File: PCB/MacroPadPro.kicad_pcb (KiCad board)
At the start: 2 copper layers, 160.7 x 77.6 mm, 119 parts, among them J1 Button, J2 Button, SW1 CPG151101S11, SW10 CPG151101S11, SW11 CPG151101S11, SW12 CPG151101S11, SW13 CPG151101S11, SW14 CPG151101S11, SW15 CPG151101S11, SW16 CPG151101S11, SW17 CPG151101S11, SW18 CPG151101S11, SW19 CPG151101S11, SW2 CPG151101S11, SW20 CPG151101S11, SW21 CPG151101S11, SW22 CPG151101S11, SW23 CPG151101S11, SW24 CPG151101S11, SW25 CPG151101S11, SW26 CPG151101S11, SW27 CPG151101S11, SW3 CPG151101S11, SW4 CPG151101S11, SW5 CPG151101S11, SW6 CPG151101S11, SW7 CPG151101S11, SW8 CPG151101S11, SW9 CPG151101S11, U1 ZL6201A33S3, U3 RP2040, Y1 TAXM12M4RKDCDT2T

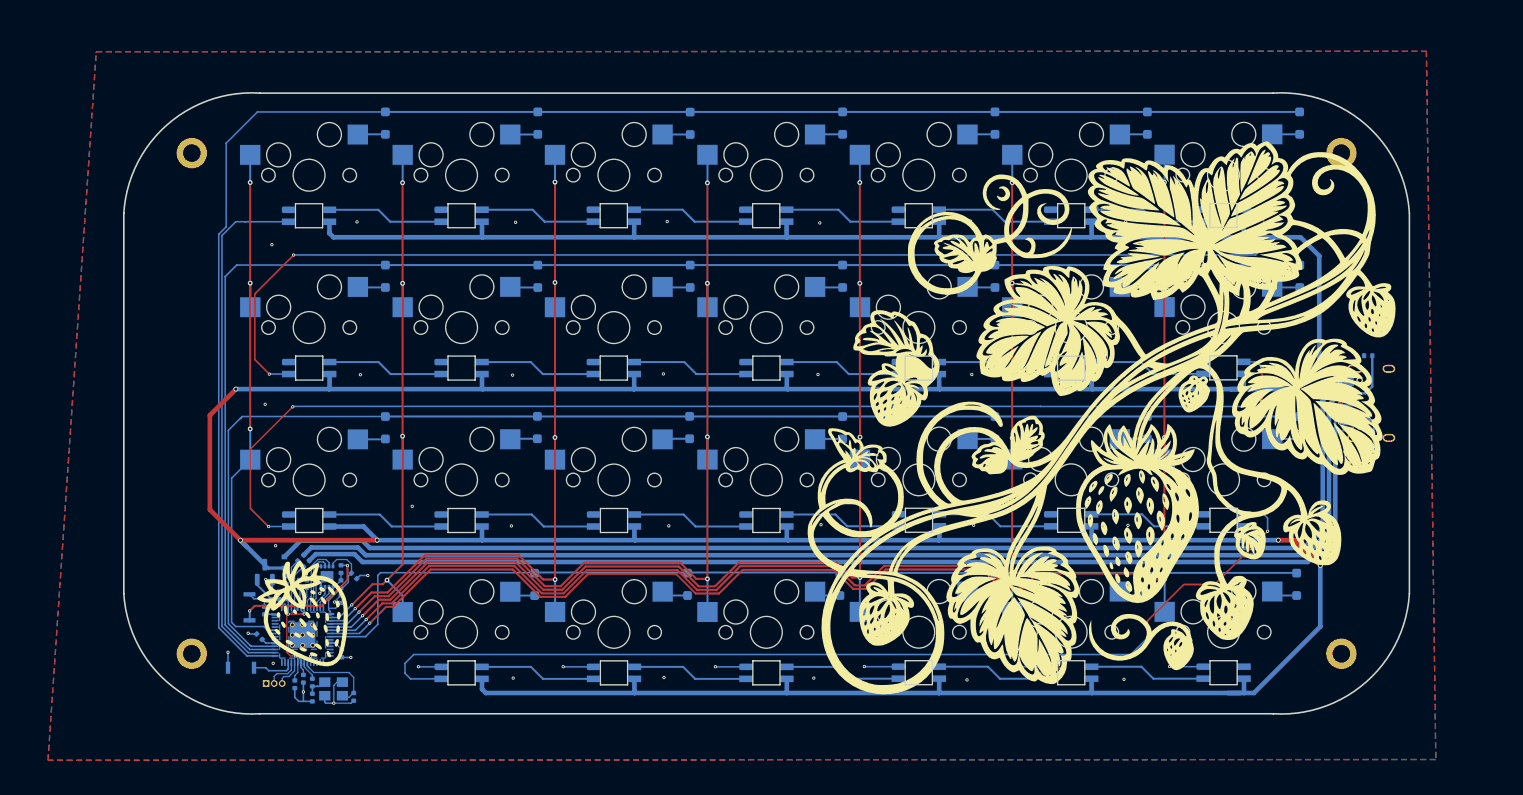
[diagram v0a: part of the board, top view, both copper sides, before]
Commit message: Updated PCB and added BOM
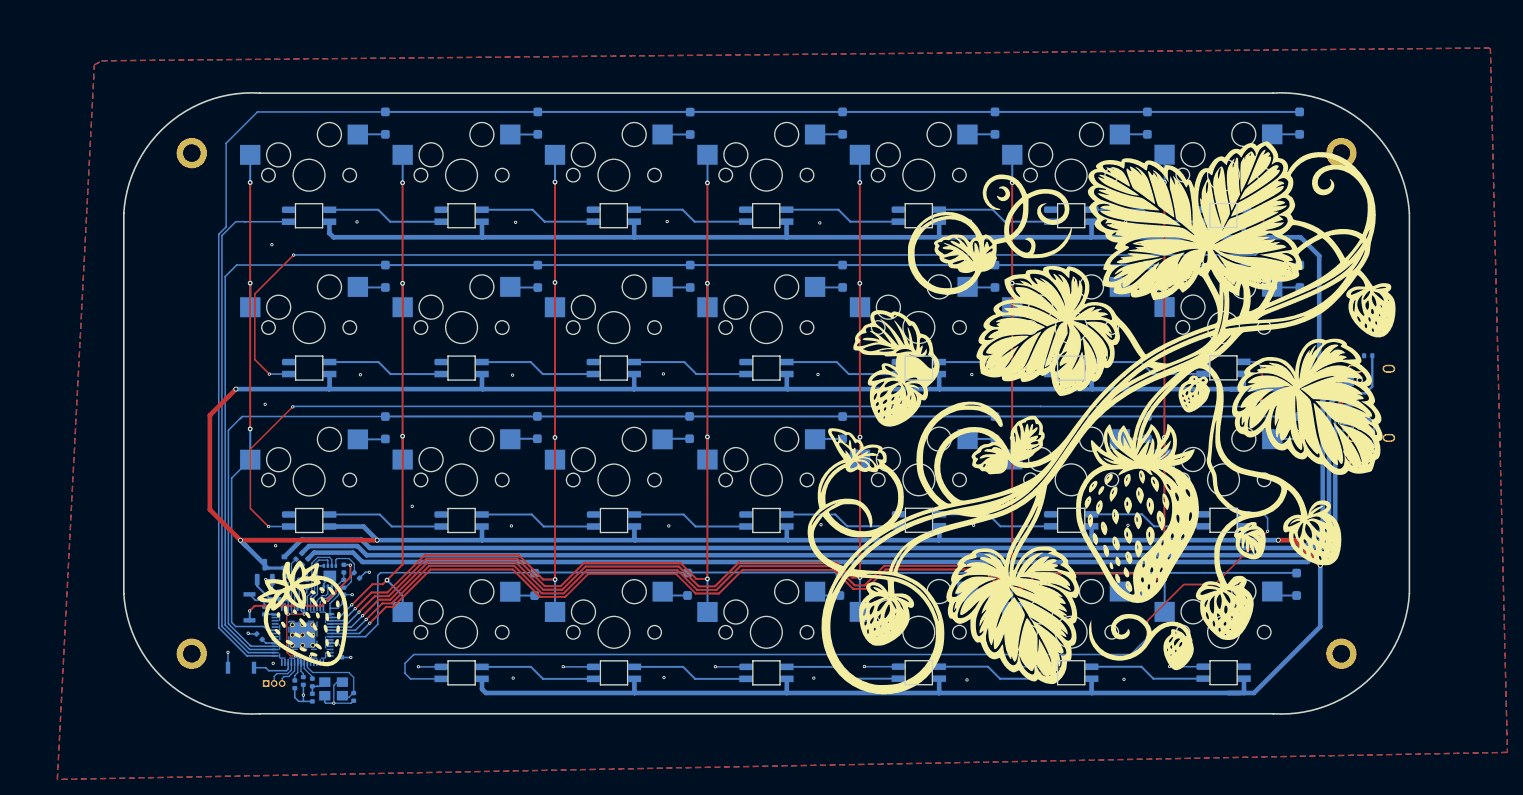
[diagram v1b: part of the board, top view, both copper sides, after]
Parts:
- C1, C10, C3, C4: value 1uf 0201 -> GRT033R60J105ME13D
- C11, C13, C14, C15, C18, C5, C6, C7, C8: value 100nf 0201 -> CSA0201X5R104K6R3ET
- C19: value 22pf 0402 -> GJM1555C1H220JB01D
- C2: value 22pF 0402 -> GJM1555C1H220JB01D
- D1: value SOD-523 General -> RB520SM-40T2R
- J1, J2: value Button -> KXT331LHS
- R1, R7: value 1K 0201 -> 0201WMF1001TEE
- R2: value 10K 0201 -> 0201WMF1002TEE
- R3, R4: value 27r 0201 -> 0201WMJ0270TEE
- R5, R6: value 5.1K 0201 -> RTT01512JTH
- hole (x4): renamed from ?; value (none) -> hole
- pin: renamed from REF**; value PinHeader_1x03_P1.00mm_Vertical -> DNP
- moved C5 0.36 mm to (107.0, 129.2)
- moved C15 0.36 mm to (105.4, 132.1)
- moved FLASH1 0.36 mm to (103.6, 129.3)
- moved R1 0.36 mm to (105.4, 128.4)
- moved R2 0.36 mm to (105.4, 130.3)
- moved R4 0.32 mm to (99.8, 126.8)
- moved R3 0.28 mm to (100.5, 127.5)
- moved C18 0.28 mm to (100.3, 142.4)
- moved C6 0.06 mm to (100.8, 130.3)
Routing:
- net +3V3: track 29.4 -> 30.8 mm
- net /QSPI_SD3: track 8.56 -> 9.48 mm
- net /QSPI_SCLK: track 7.34 -> 8.18 mm

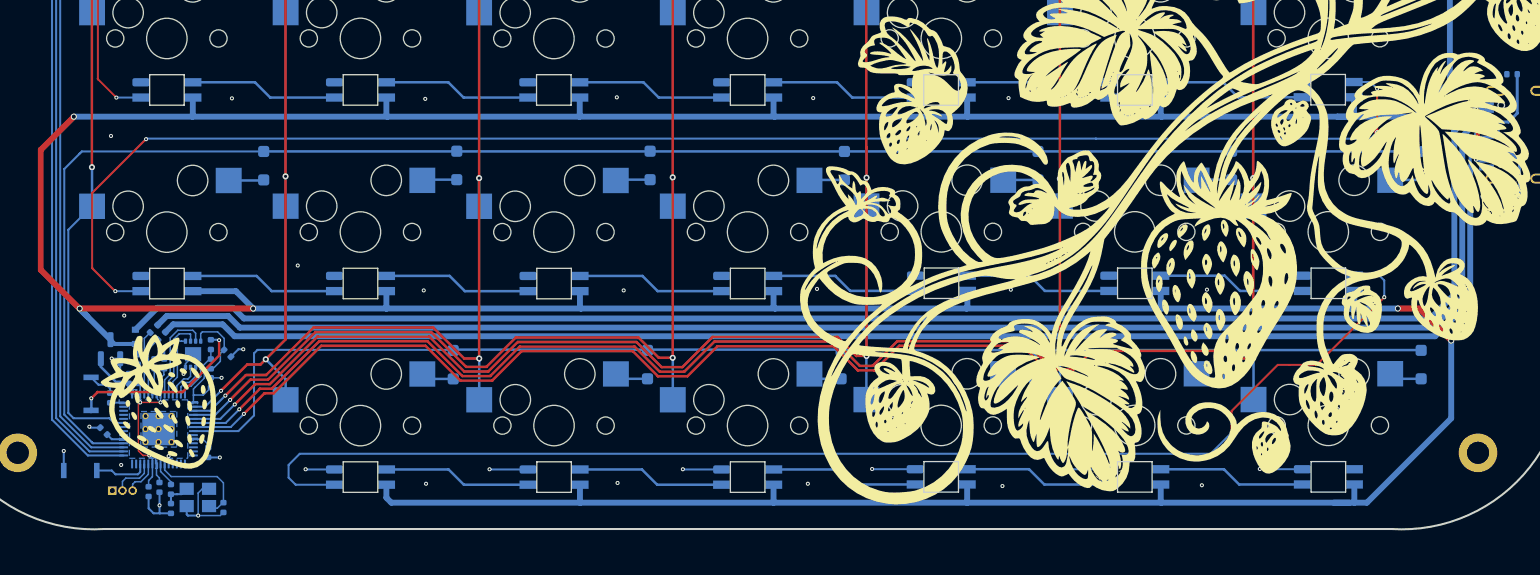
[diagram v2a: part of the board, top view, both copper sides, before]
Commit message: Updated PCB design to fix GND fault and update BOM components
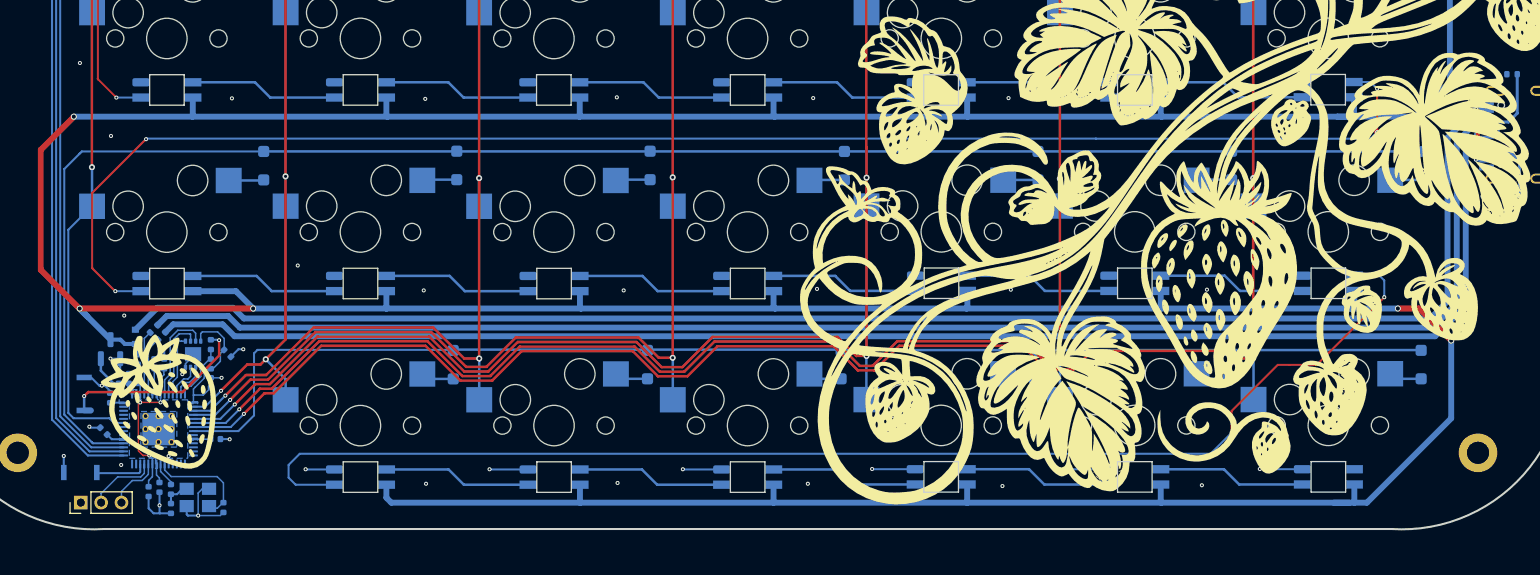
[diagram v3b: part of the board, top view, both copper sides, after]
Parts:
- U1: value ZL6201A33S3 -> AP2210N-3.3TRG1
- pin: footprint Connector_PinHeader_1.00mm:PinHeader_1x03_P1.00mm_Vertical -> Connector_PinHeader_2.00mm:PinHeader_1x03_P2.00mm_Vertical
- moved pin 3.31 mm to (92.6, 143.9)
- moved C8 1.50 mm to (105.8, 137.7), turned to 0 degrees
- moved J2 0.68 mm to (92.9, 133.2)
- moved J1 0.20 mm to (92.5, 141.0)
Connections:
- C2 pad 1: (no net) -> Net-(U3-XOUT)
- R7 pad 1: (no net) -> Net-(U3-XOUT)
- Y1 pad 3: (no net) -> Net-(U3-XOUT)
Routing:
- net Net-(U3-XOUT): track 2.44 -> 5.89 mm
- net (no net): track 3.45 -> 0.00 mm
- net /SWD: track 4.72 -> 7.30 mm
- net /SWCLK: track 3.60 -> 5.46 mm
- net /~{USB_BOOT}: track 17.8 -> 19.3 mm
- net GND: track 59.9 -> 59.3 mm, vias 47 -> 48
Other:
- board text added: "BOOT"
- board text added: "Model: Fragaria-27 (Hotswap - RP2040) v2.0 Designed by: James Gzowski (github.com/gzowski)"
- board text added: "RESET"
- board text removed: "Model: Fragaria-27 (Hotswap - RP2040) Designed by: James Gzowski (github.com/gzowski)"
